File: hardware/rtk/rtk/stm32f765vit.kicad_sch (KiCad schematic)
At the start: 24 parts, among them J6 MEM2052-00-195-00-A_REVA, J7 Conn_01x04_Pin, J8 Conn_01x01_Pin, J9 Conn_01x08_Pin, U3 STM32F765VITx, U5 ESP32-S3-ZERO, U6 CORE1262-868M, U7 LSM6DSOX, Y1 ASTX-H11-16.000MHZ-T

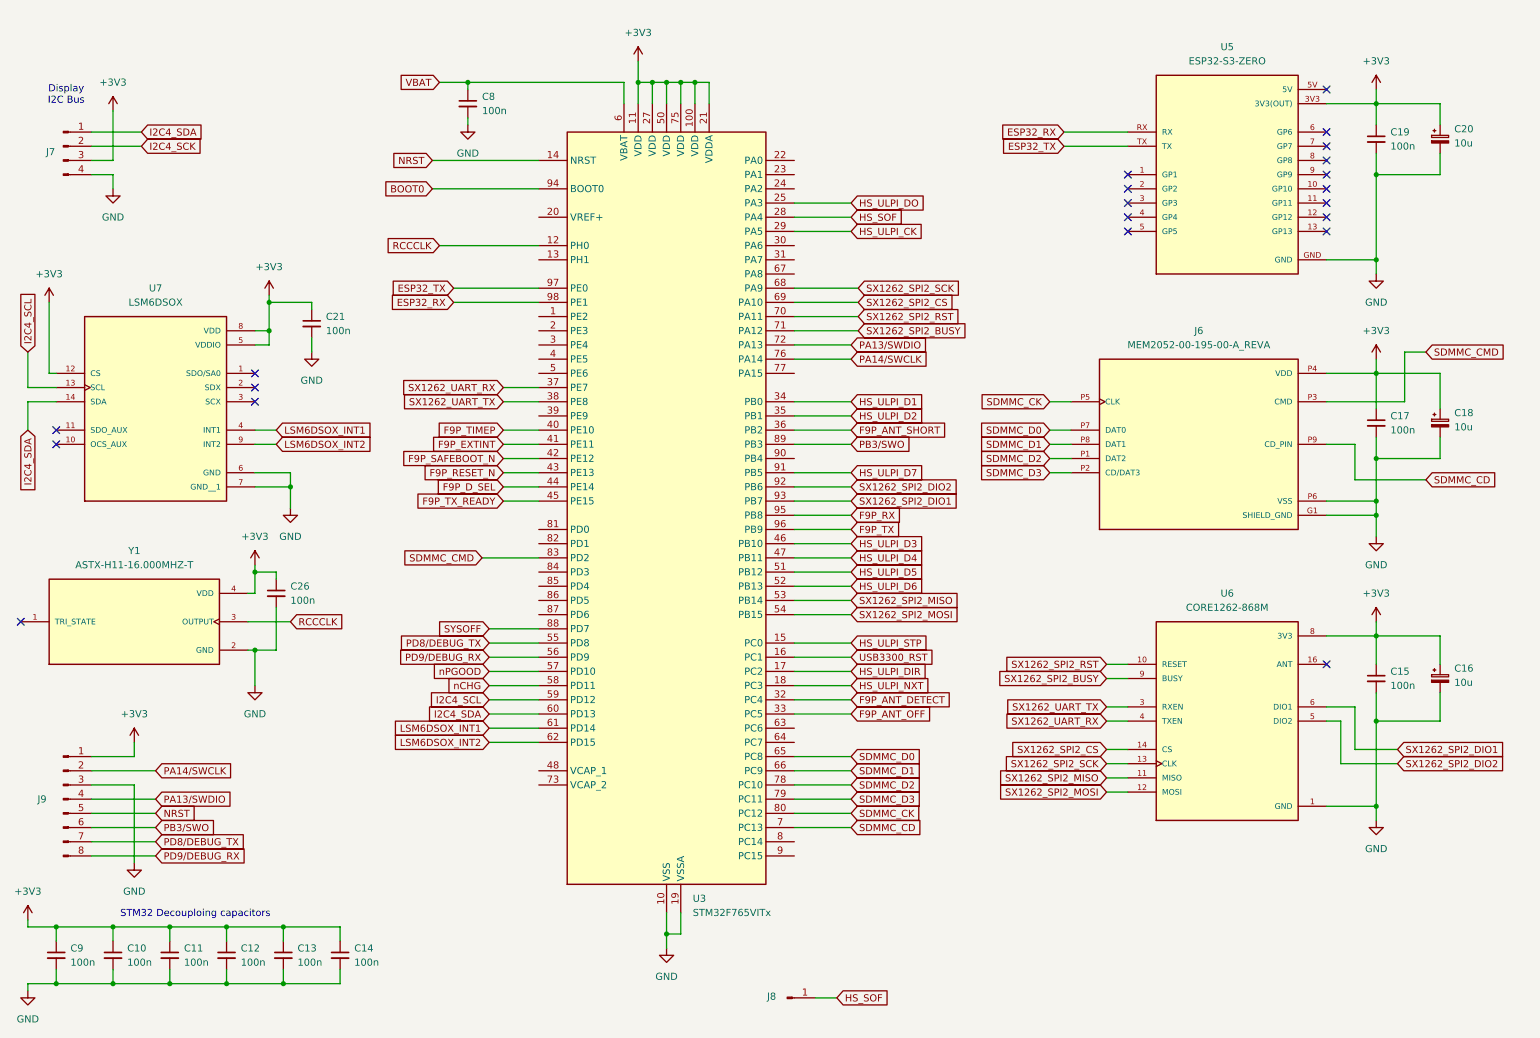
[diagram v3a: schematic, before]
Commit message: STM32F765VIT sheet review fixes (#182)
- VBAT tied to +3V3 (not raw LiPo)
- CORE1262 RXEN/TXEN reassigned to PC6/PC7 GPIO outputs (init low)
- I2C4 external 4k7 pull-ups added on SCL/SDA
- BOOT0 pull-down + test point added
- LSM6DSOX CS tied to +3V3, SDO/SA0 tied to GND (addr 0x6A)
- ESP32-S3-ZERO: 5V NC, powered via 3V3 rail; GP1-GP5 wired to PE2-PE6
- nPGOOD/nCHG/SYSOFF added to STM32 sheet
- MMC5603NJ sub-board connector added (I2C4, 2x GPIO, 3V3, GND)
- rtk-base.ioc: PC6/PC7 RXEN/TXEN, PE2-PE6 spare, PD7/PD10/PD11

Co-Authored-By: Claude Sonnet 4.6 <noreply@anthropic.com>
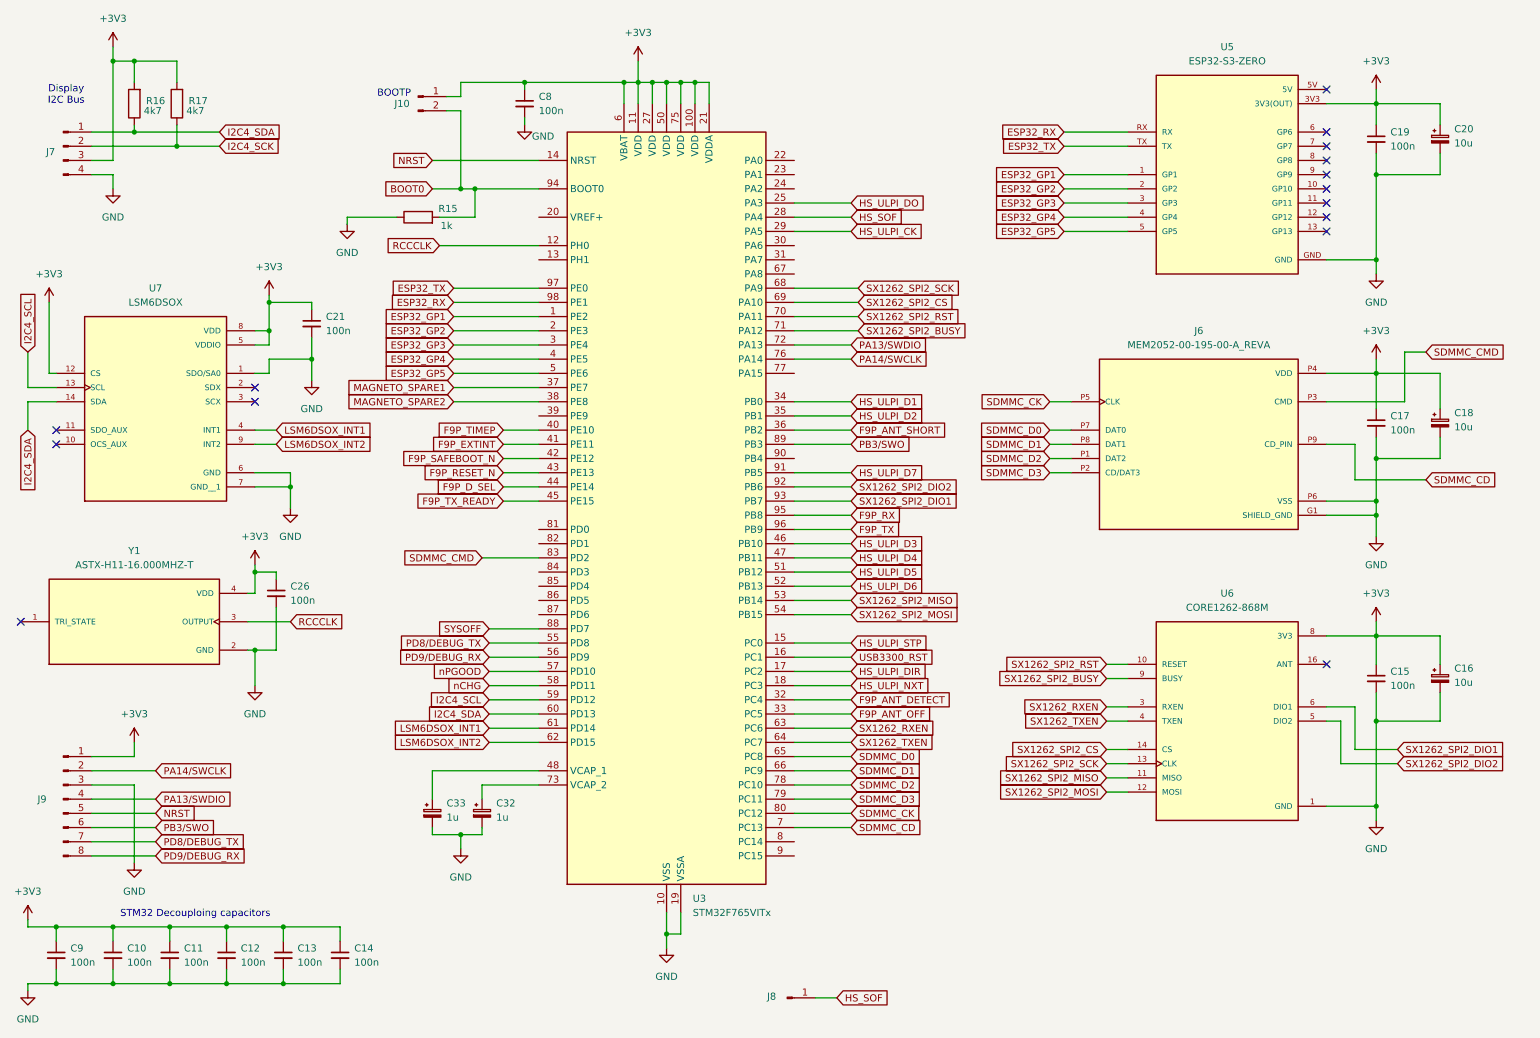
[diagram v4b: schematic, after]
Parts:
- added C32, C33: 1u, Capacitor_SMD:C_0805_2012Metric_Pad1.18x1.45mm_HandSolder, symbol Device:C_Polarized_Small
- added J10: Conn_01x02_Pin, Connector_PinHeader_2.54mm:PinHeader_1x02_P2.54mm_Vertical, symbol Connector:Conn_01x02_Pin
- added R15: 1k, Resistor_SMD:R_0805_2012Metric_Pad1.20x1.40mm_HandSolder, symbol Device:R
- added R16, R17: 4k7, Resistor_SMD:R_0805_2012Metric_Pad1.20x1.40mm_HandSolder, symbol Device:R
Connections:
- net VBAT is gone; now on net +3V3: C8.1, U3.6 (VBAT)
- net +3V3: now also J10.1 (Pin_1), R16.2, R17.2
- net BOOT0: now also J10.2 (Pin_2), R15.2
- net GND: now also U7.1 (SDO/SA0), C32.2, C33.2, R15.1
- net I2C4_SCK: now also R17.1
- net I2C4_SDA: now also R16.1
- net ESP32_GP1: now reaches U5.1 (GP1)
- net ESP32_GP1: now also U3.1 (PE2)
- net ESP32_GP2: now reaches U5.2 (GP2)
- net ESP32_GP2: now also U3.2 (PE3)
- net ESP32_GP3: now reaches U5.3 (GP3)
- net ESP32_GP3: now also U3.3 (PE4)
- net ESP32_GP4: now reaches U5.4 (GP4)
- net ESP32_GP4: now also U3.4 (PE5)
- net ESP32_GP5: now reaches U5.5 (GP5)
- net ESP32_GP5: now also U3.5 (PE6)
- net at U3.48 (VCAP_1): now also C33.1
- net SX1262_RXEN: now reaches U3.63 (PC6)
- net SX1262_RXEN: now also U6.3 (RXEN)
- net SX1262_TXEN: now reaches U3.64 (PC7)
- net SX1262_TXEN: now also U6.4 (TXEN)
- net at U3.73 (VCAP_2): now also C32.1
- net SX1262_UART_RX renamed MAGNETO_SPARE1
- net MAGNETO_SPARE1: no longer U6.4 (TXEN)
- net SX1262_UART_TX renamed MAGNETO_SPARE2
- net MAGNETO_SPARE2: no longer U6.3 (RXEN)
- no-connect marks 21 -> 15
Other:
- note added: "BOOTP"
- moved on the sheet: C8
